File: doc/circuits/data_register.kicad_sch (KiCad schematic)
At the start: 12 parts, among them U1 74LS193, U10 74LS32, U11 74LS32, U12 74LS04, U13 74LS193, U3 74LS245, U4 74LS04, U5 74LS04, U6 74LS32, U7 74LS245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

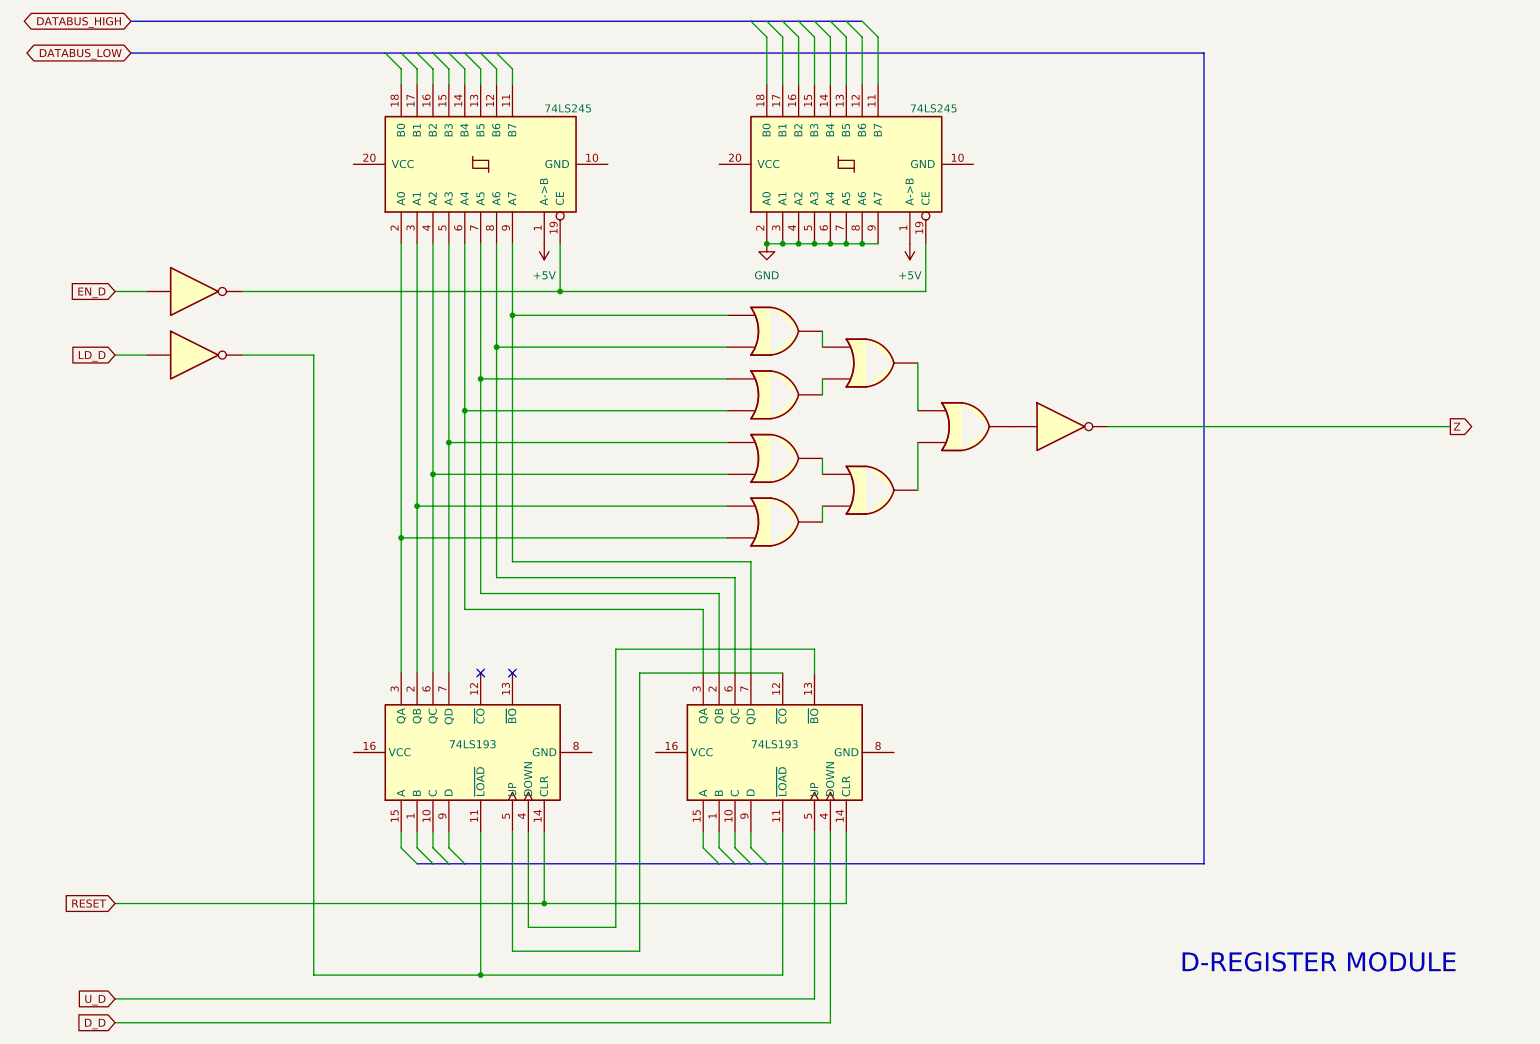
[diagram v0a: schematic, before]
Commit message: documented data and datapointer registers
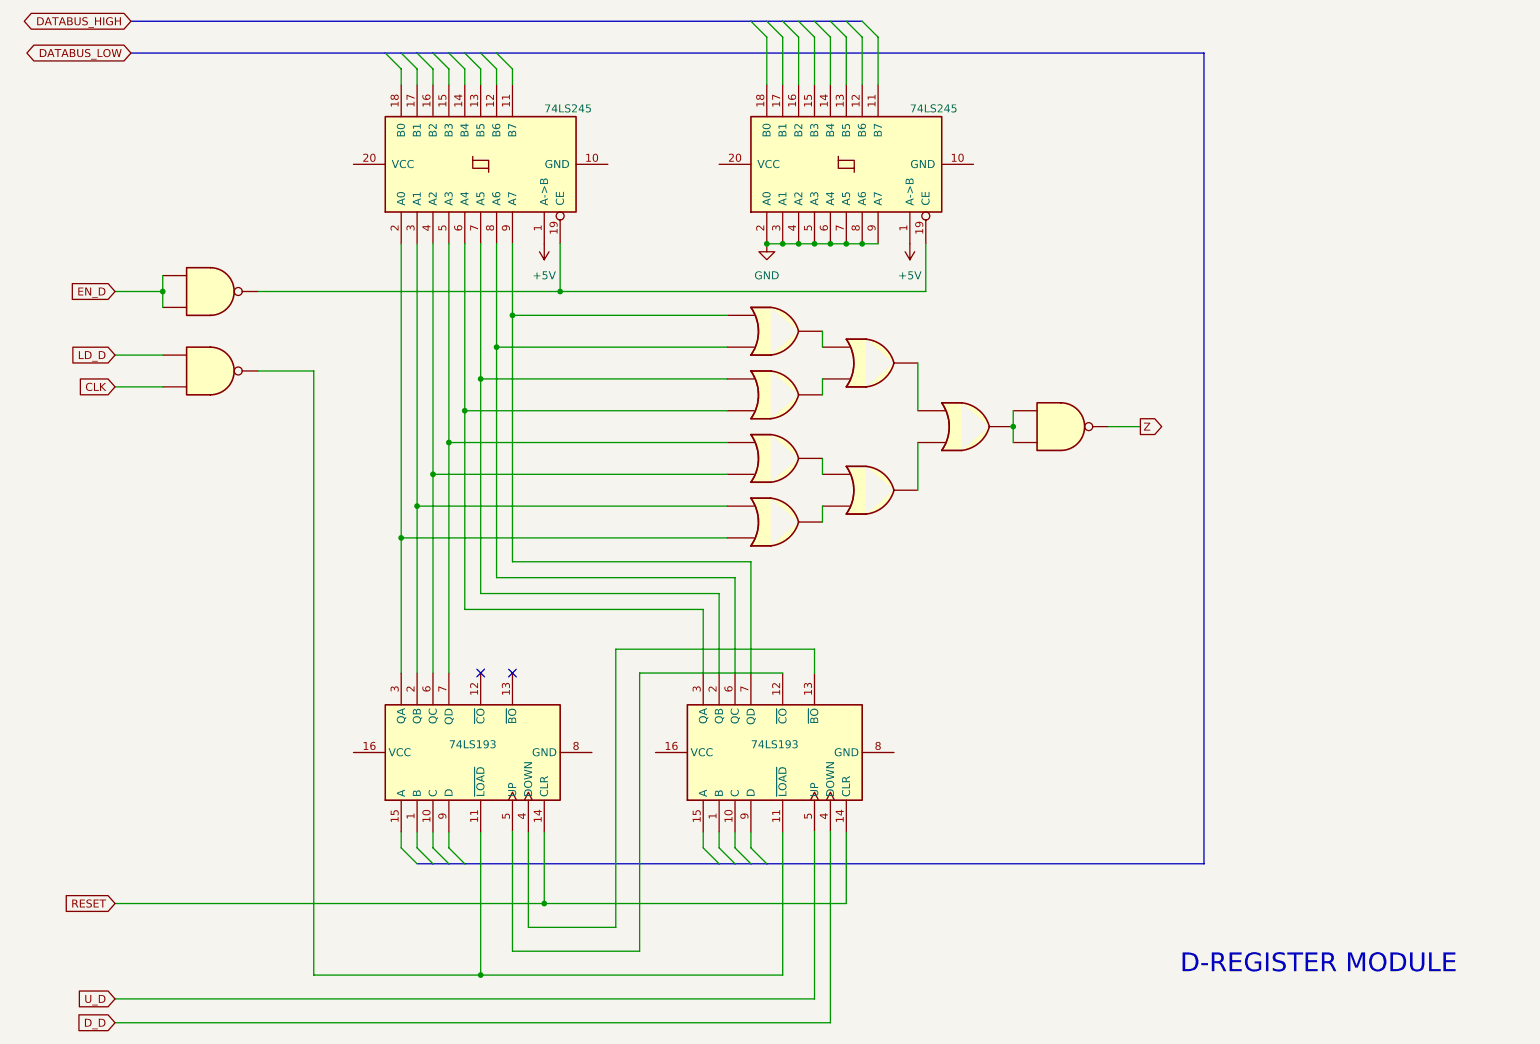
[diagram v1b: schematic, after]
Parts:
- removed U12, U4, U5: 74LS04, symbol 74xx:74LS04
- added U2, U4, U5: 74LS00, symbol 74xx:74LS00
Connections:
- net EN_D: now also U2.1, U2.2
- net LD_D: now also U5.1
- net Z: now also U4.3
- net at U3.19 (CE), U7.19 (CE): now also U2.3
- net at U1.11 (~{LOAD}), U13.11 (~{LOAD}): now also U5.3
- net at U11.3: now also U4.1, U4.2
- new net CLK: U5.2
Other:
- company: (none) -> J. Heit

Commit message: more documentation
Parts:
- removed U10, U11, U6, U8, U9: 74LS32, symbol 74xx:74LS32
- removed U4: 74LS00, symbol 74xx:74LS00
- added U12: 4078, symbol 4xxx_IEEE:4078
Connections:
- net +5V: now also U12.7 (Vss)
- net GND: now also U12.14 (Vdd)
- net Z: now also U12.13
- net at U1.3 (QA), U3.2 (A0): now also U12.12
- net at U1.2 (QB), U3.3 (A1): now also U12.11
- net at U1.6 (QC), U3.4 (A2): now also U12.10
- net at U1.7 (QD), U3.5 (A3): now also U12.9
- net at U13.3 (QA), U3.6 (A4): now also U12.5
- net at U13.2 (QB), U3.7 (A5): now also U12.4
- net at U13.6 (QC), U3.8 (A6): now also U12.3
- net at U13.7 (QD), U3.9 (A7): now also U12.2
- no-connect marks 2 -> 3

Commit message: more documentation
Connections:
- net Z renamed SET_Z
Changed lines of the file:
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@@
 		)
 	)
-	(global_label "Z"
+	(global_label "SET_Z"
 		(shape output)
 		(at 181.61 95.25 0)
@@
 		)
 		(property "Intersheetrefs" "${INTERSHEET_REFS}"
-			(at 185.8047 95.25 0)
+			(at 190.0984 95.25 0)
 			(effects
 				(font
